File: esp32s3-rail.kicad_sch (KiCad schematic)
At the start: 53 parts, among them J1 Conn_01x06, J2 Conn_01x06, J3 USB_C_Receptacle_USB2.0_16P, J4 RJ45_Wuerth_7499010121A, J5 490107670612, J6 Conn_02x20_Odd_Even, U1 R-78E5.0-0.5, U2 AMS1117-3.3, U3 WE-TVS-82400102, U4 W5500, U5 ESP32-S3-MINI-1U, Y1 25M, Y2 32.768 kHz

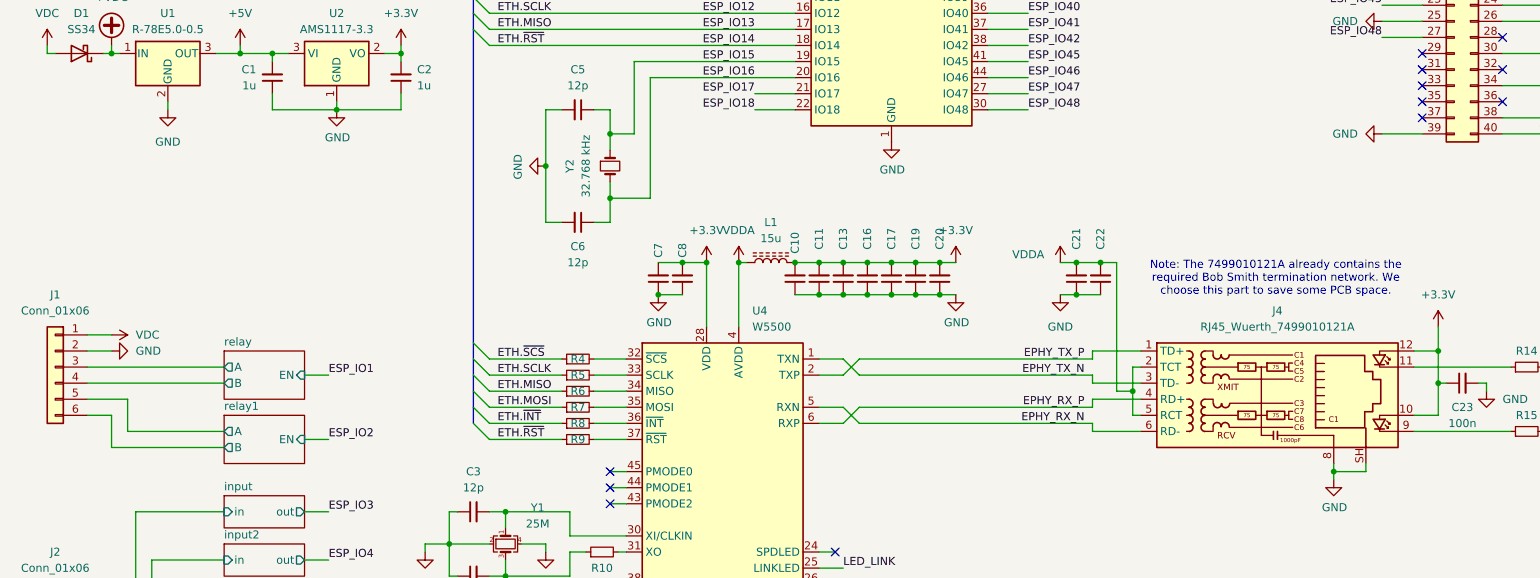
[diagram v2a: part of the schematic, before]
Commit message: Assign footprints.
Signed-off-by: Dominik Bayerl <dominik.bayerl@carissma.eu>
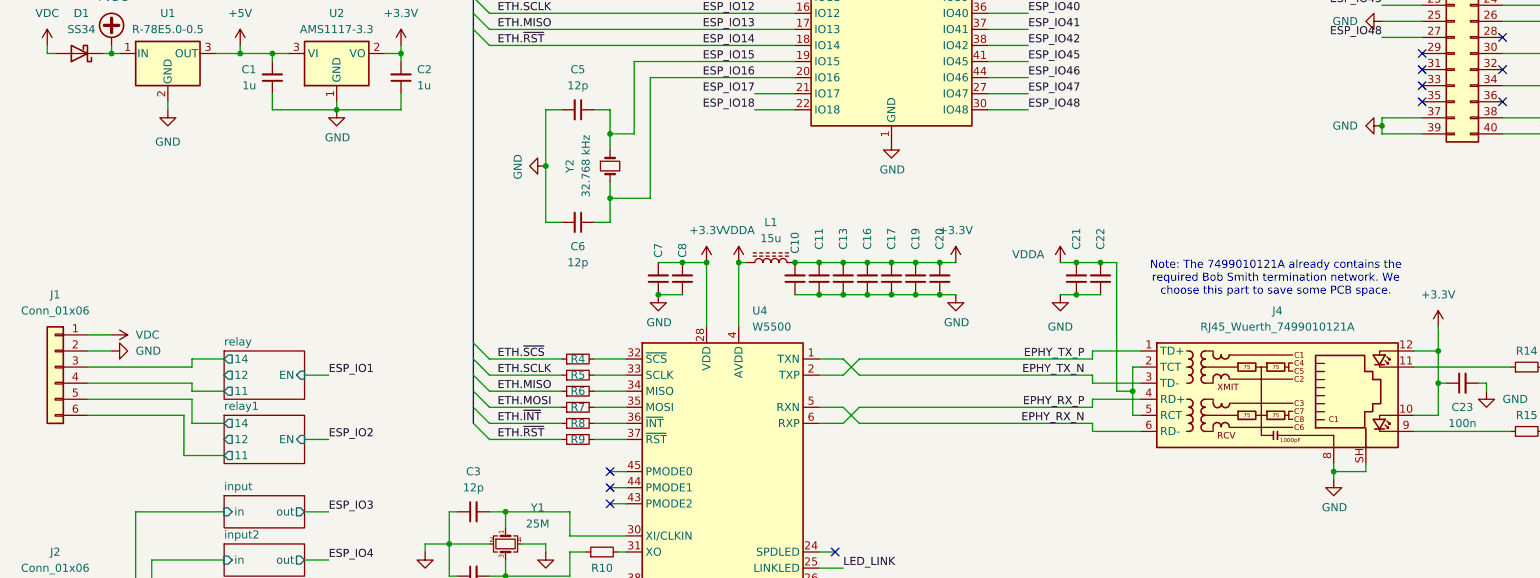
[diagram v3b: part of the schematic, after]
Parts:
- D1: footprint Diode_SMD:D_SMC_Handsoldering -> Diode_SMD:D_SOD-123
- J1, J2: footprint (none) -> Connector_Phoenix_MSTB:PhoenixContact_MSTBA_2,5_6-G_1x06_P5.00mm_Horizontal
- R1, R12, R2, R3: footprint Resistor_SMD:R_1206_3216Metric -> Resistor_SMD:R_0603_1608Metric_Pad0.98x0.95mm_HandSolder
- R10, R11, R13, R14, R15, R4, R5, R6, R7, R8, R9: footprint Resistor_SMD:R_0603_1608Metric -> Resistor_SMD:R_0603_1608Metric_Pad0.98x0.95mm_HandSolder
- Y1: footprint (none) -> Crystal:Crystal_SMD_3225-4Pin_3.2x2.5mm_HandSoldering
- Y2: footprint Crystal:Crystal_SMD_EuroQuartz_EQ161-2Pin_3.2x1.5mm_HandSoldering -> Crystal:Crystal_SMD_3215-2Pin_3.2x1.5mm
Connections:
- net GND: now also J6.37 (Pin_37)
- net relay/A renamed relay/14
- net relay/B renamed relay/11
- net relay1/A renamed relay1/14
- net relay1/B renamed relay1/11
- no-connect marks 21 -> 20
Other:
- sheet relay ports: added 11, 12, 14; removed A, B
- sheet relay1 ports: added 11, 12, 14; removed A, B

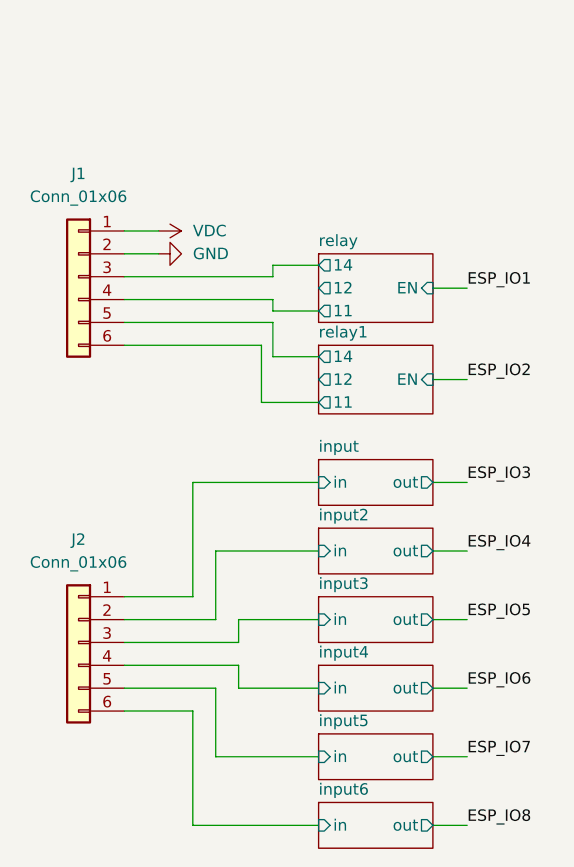
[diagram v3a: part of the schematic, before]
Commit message: Update stacking header.
Signed-off-by: Dominik Bayerl <dominik.bayerl@carissma.eu>
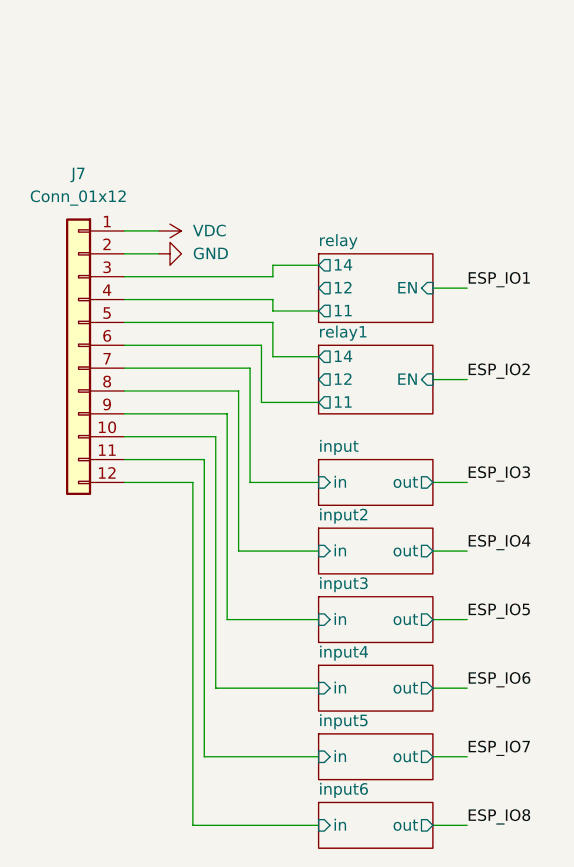
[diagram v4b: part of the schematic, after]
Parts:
- removed J1, J2: Conn_01x06, Connector_Phoenix_MSTB:PhoenixContact_MSTBA_2,5_6-G_1x06_P5.00mm_Horizontal, symbol Connector_Generic:Conn_01x06
- added J7: Conn_01x12, Connector_Molex:Molex_SPOX_5268-12A_1x12_P2.50mm_Horizontal, symbol Connector_Generic:Conn_01x12
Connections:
- net GND: now also J7.2 (Pin_2)
- net VDC: now also J7.1 (Pin_1)
- net input/in: now also J7.7 (Pin_7)
- net input2/in: now also J7.8 (Pin_8)
- net input3/in: now also J7.9 (Pin_9)
- net input4/in: now also J7.10 (Pin_10)
- net input5/in: now also J7.11 (Pin_11)
- net input6/in: now also J7.12 (Pin_12)
- net relay/11: now also J7.4 (Pin_4)
- net relay/14: now also J7.3 (Pin_3)
- net relay1/11: now also J7.6 (Pin_6)
- net relay1/14: now also J7.5 (Pin_5)
